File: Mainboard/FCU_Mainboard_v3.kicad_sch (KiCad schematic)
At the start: 12 parts, among them U5 ATMega2560

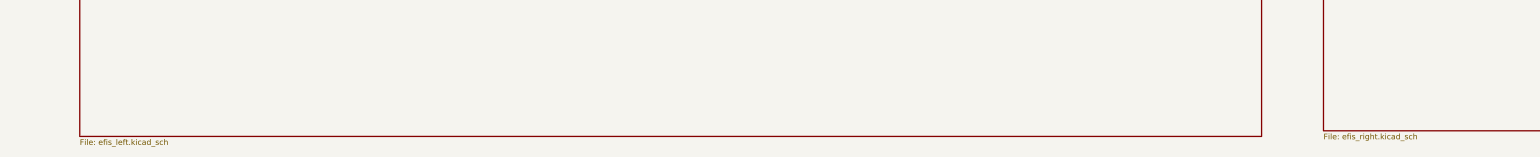
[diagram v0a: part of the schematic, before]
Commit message: Fix the swapped EFIS filenames and rename the backlight nets to +5V
Two naming defects, no electrical change on any board.

EFIS sheets
-----------
The root sheet pointed EFIS_LEFT at efis_right.kicad_sch and EFIS_RIGHT at
efis_left.kicad_sch. The schematic was correct, since the file behind the
LEFT sheet did hold the L_* signals, but the filenames said the opposite and
anyone reading the files from outside KiCad would have been misled.

The two files are swapped and every reference follows: the sheet properties
in the root schematic and the 49 sheetfile entries the footprints carry on
the board. Each file now matches the sheet that loads it.

  netlist   198 nets, 135 components, not one node moved
  ERC       0 violations
  DRC       6 violations, all cosmetic, 0 unconnected, 0 parity issues

Backlight nets
--------------
Every net in the backlighting chain was called +9V while carrying 5 V, on
all four boards. The white LEDs sit behind 91 Ω: at 5 V that is 21 mA, right
at the rating for a 1206 white LED, while 9 V would put them at 65 mA. The
name was a leftover from an earlier design and was the kind of label that
eventually makes someone connect the wrong supply.

Renamed across Korry_Large, Korry_Small, Backlighting_Dimmer and
Backlighting_LEDModule, in both the schematics and the boards: the power
symbol, its value, which is what actually names the net, and the net entries
on the copper. 88 occurrences. None of those boards had a +5V net already,
so nothing was merged.

Verified against the state committed a moment ago: ERC and DRC counts are
identical on all four boards, before and after, and no board gained or lost
a connection.

The Readme drops these two entries and gains the defects that surfaced while
checking: the Backlighting_Dimmer footprints carry their reference in the
value field instead of the schematic value, so a BOM read from that board is
wrong; its terminal block footprint no longer exists in the KiCad library;
four texts on the Korry_Large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
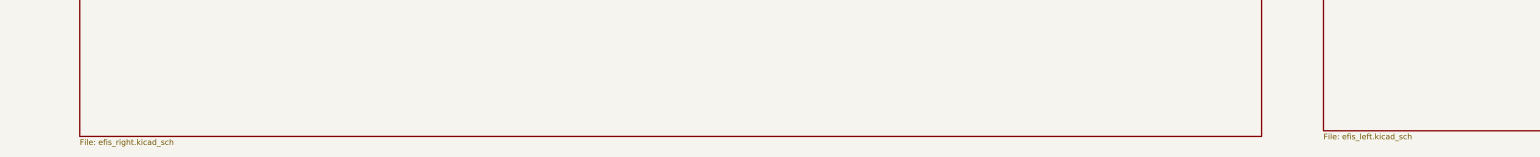
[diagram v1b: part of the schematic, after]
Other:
- sheet EFIS_LEFT: file efis_right.kicad_sch -> efis_left.kicad_sch
- sheet EFIS_RIGHT: file efis_left.kicad_sch -> efis_right.kicad_sch
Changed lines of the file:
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@@
 			)
 		)
-		(property "Sheetfile" "efis_right.kicad_sch"
+		(property "Sheetfile" "efis_left.kicad_sch"
 			(at 612.14 432.3846 0)
 			(show_name yes)
@@
 			)
 		)
-		(property "Sheetfile" "efis_left.kicad_sch"
+		(property "Sheetfile" "efis_right.kicad_sch"
 			(at 331.47 433.6546 0)
 			(show_name yes)

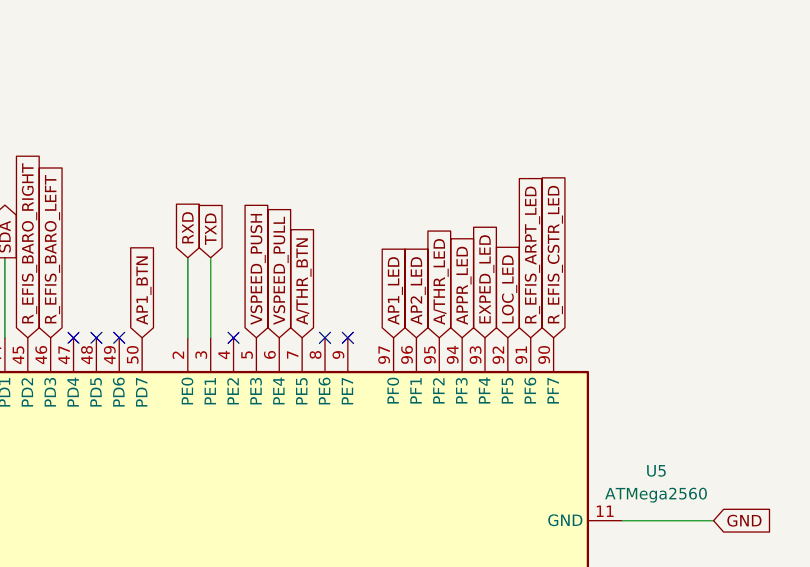
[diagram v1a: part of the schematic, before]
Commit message: Name the two autopilot lamp nets after the right autopilot
J10 porta la serigrafia AP2 e aveva sopra AP1_LED con AP2_BTN; J11 porta AP1
e aveva AP2_LED con AP1_BTN. Su un Airbus i due autopiloti sono indipendenti,
quindi ogni connettore deve portare la lampada e il pulsante dello stesso.

Il difetto sta solo nei nomi: le due reti LED arrivano ai pin 96 e 97 del
Mega, adiacenti, e ognuna era gia' cablata al connettore giusto. Scambiare i
due nomi rende coerenti schema, serigrafia e rame senza spostare un
millimetro di pista, e senza toccare la configurazione MobiFlight, che
ragiona per numero di pin.

Ora: J10 (AP2) = AP2_LED + AP2_BTN, J11 (AP1) = AP1_LED + AP1_BTN.
ERC 0, DRC 0, parita' 0.

Co-Authored-By: Claude Opus 5 <noreply@anthropic.com>
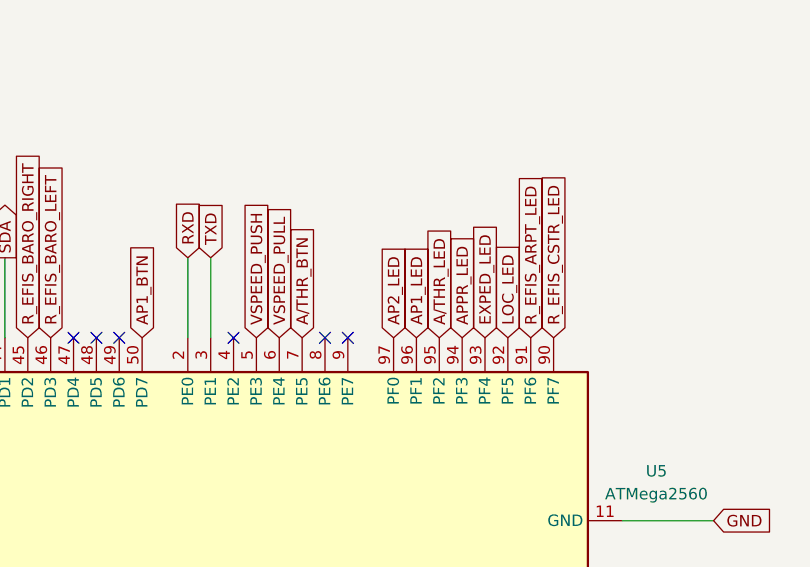
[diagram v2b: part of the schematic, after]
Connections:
- net AP1_LED: now also U5.96 (PF1); no longer U5.97 (PF0)
- net AP2_LED: now also U5.97 (PF0); no longer U5.96 (PF1)
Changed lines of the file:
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@@
 		)
 	)
-	(global_label "AP1_LED"
+	(global_label "AP2_LED"
 		(shape input)
 		(at 212.09 87.63 90)
@@
 		)
 	)
-	(global_label "AP2_LED"
+	(global_label "AP1_LED"
 		(shape input)
 		(at 214.63 87.63 90)
